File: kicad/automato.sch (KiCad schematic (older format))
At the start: 72 parts, among them J1 USB_C_Receptacle, J10 QWIIC 0, J2 LiPo, J3 Conn_01x07_Male, J4 Screw_Terminal_01x15, J5 USB_C_Receptacle, J6 Conn_Coaxial, J7 UART2 0, J8 Micro_SD_Card_Det, J9 UART2 1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

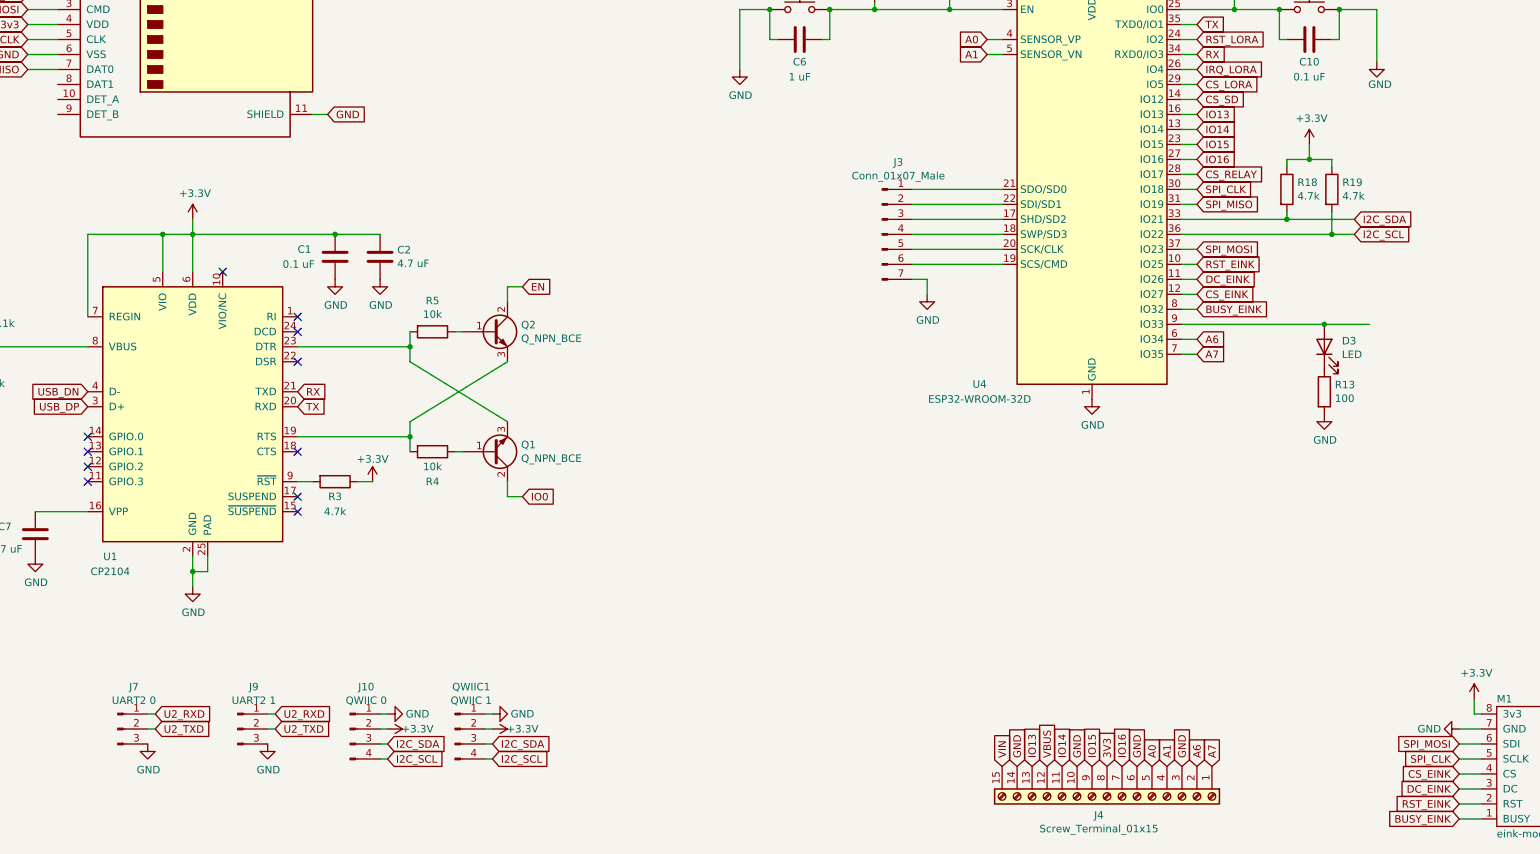
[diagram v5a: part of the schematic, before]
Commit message: adding more jst connectors, moving pin assignments
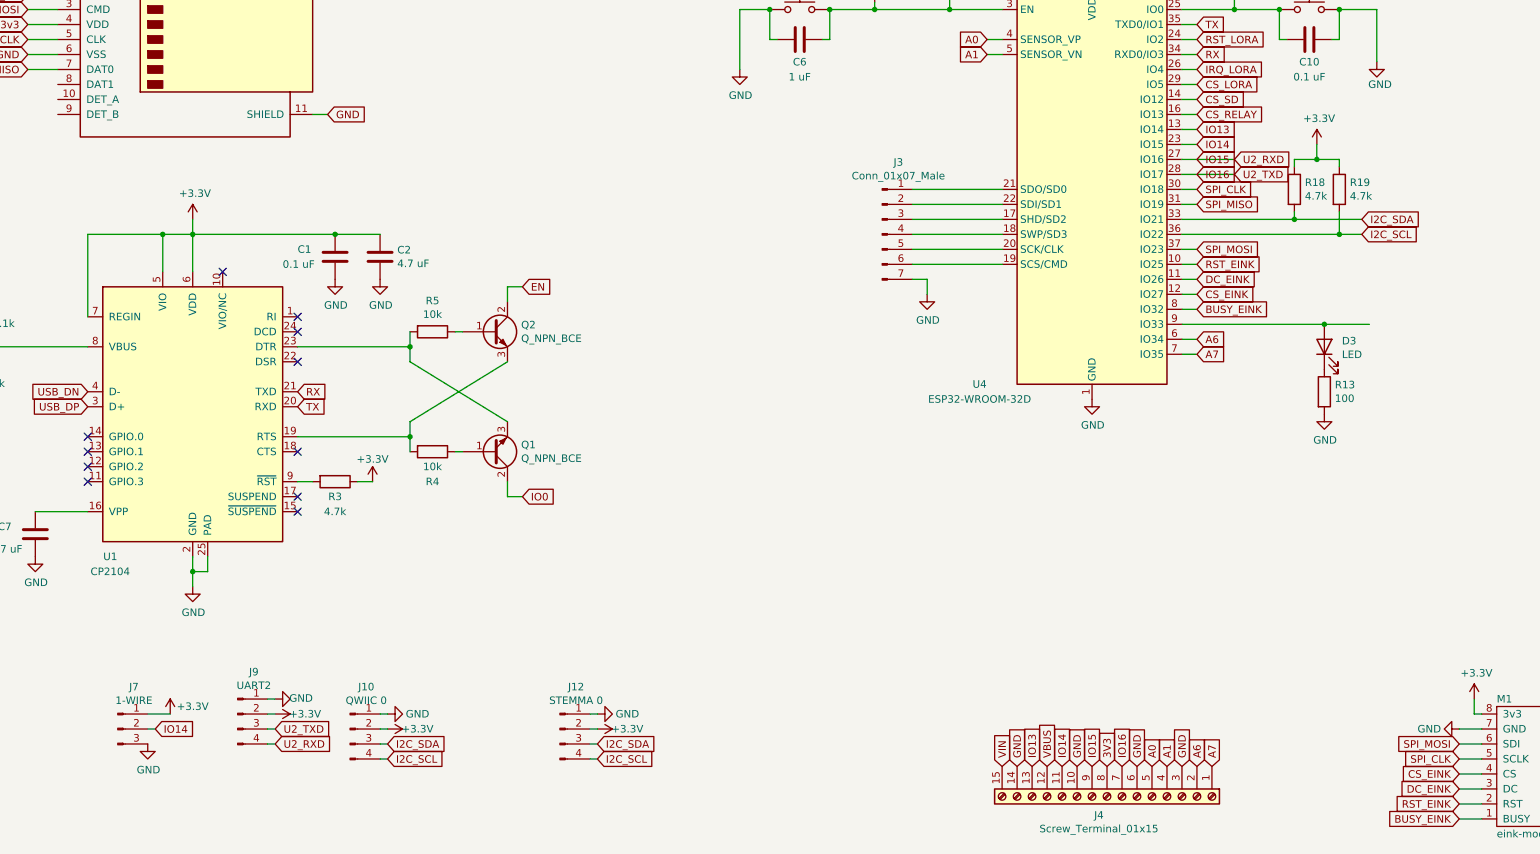
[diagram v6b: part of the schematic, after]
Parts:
- removed J9: UART2 1, Connector_JST:JST_PH_S3B-PH-SM4-TB_1x03-1MP_P2.00mm_Horizontal, symbol Connector:Conn_01x03_Male
- removed QWIIC1: QWIIC 1, Connector_JST:JST_SH_SM04B-SRSS-TB_1x04-1MP_P1.00mm_Horizontal, symbol Connector:Conn_01x04_Male
- added J12: STEMMA 0, Connector_JST:JST_PH_S4B-PH-SM4-TB_1x04-1MP_P2.00mm_Horizontal, symbol Connector:Conn_01x04_Male
- added J9: UART2, Connector_JST:JST_PH_S4B-PH-SM4-TB_1x04-1MP_P2.00mm_Horizontal, symbol Connector:Conn_01x04_Male
- J6: footprint Connector_Coaxial:SMA_Wurth_60312002114503_Vertical -> Connector_Coaxial:SMA_Molex_73251-1153_EdgeMount_Horizontal
- J7: value UART2 0 -> 1-WIRE
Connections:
- net +3V3: now also J7.1 (Pin_1), J12.2 (Pin_2), J9.2 (Pin_2)
- net CS_RELAY: now also U4.16 (IO13); no longer U4.28 (IO17)
- net GND: now also J12.1 (Pin_1), J9.1 (Pin_1)
- net I2C_SCL: now also J12.4 (Pin_4)
- net I2C_SDA: now also J12.3 (Pin_3)
- net IO13: now also U4.13 (IO14); no longer U4.16 (IO13)
- net IO14: now also J7.2 (Pin_2), U4.23 (IO15); no longer U4.13 (IO14)
- net IO15: now also JP1.3 (B), U4.27 (IO16), J9.4 (Pin_4); no longer U4.23 (IO15)
- net IO16: now also JP2.3 (B), U4.28 (IO17), J9.3 (Pin_3); no longer U4.27 (IO16)
- removed net U2_RXD: J7.1 (Pin_1), JP1.3 (B)
- removed net U2_TXD: J7.2 (Pin_2), JP2.3 (B)
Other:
- moved on the sheet: R18, R19
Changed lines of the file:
@@
 Wire Wire Line
 	9550 5350 9650 5350
-Text GLabel 9650 5350 2    50   Input ~ 0
-CS_SD
 Text GLabel 9650 5950 2    50   Input ~ 0
 SPI_CLK
 Text GLabel 9650 6050 2    50   Input ~ 0
 SPI_MISO
-Text GLabel 10700 6150 2    50   Input ~ 0
+Text GLabel 10750 6150 2    50   Input ~ 0
 I2C_SDA
-Text GLabel 10700 6250 2    50   Input ~ 0
+Text GLabel 10750 6250 2    50   Input ~ 0
 I2C_SCL
 Text GLabel 9650 6350 2    50   Input ~ 0
 SPI_MOSI
-Text GLabel 9650 5750 2    50   Input ~ 0
-IO16
-Text GLabel 9650 5450 2    50   Input ~ 0
-IO13
-Text GLabel 9650 5550 2    50   Input ~ 0
-IO14
 Text GLabel 9650 6950 2    50   Input ~ 0
 A6
@@
 	9550 5650 9650 5650
 Wire Wire Line
-	9550 5750 9650 5750
-Wire Wire Line
-	9550 5850 9650 5850
-Wire Wire Line
 	9550 5950 9650 5950
 Wire Wire Line
 	9550 6050 9650 6050
-Wire Wire Line
-	9550 6150 10250 6150
 Wire Wire Line
 	9550 6350 9650 6350
@@
 L Device:R R18
 U 1 1 6005DDCE
-P 10250 5950
-F 0 "R18" H 10320 5996 50  0000 L CNN
-F 1 "4.7k" H 10320 5905 50  0000 L CNN
-F 2 "Resistor_SMD:R_0805_2012Metric" V 10180 5950 50  0001 C CNN
-F 3 "~" H 10250 5950 50  0001 C CNN
-	1    10250 5950
+P 10300 5950
+F 0 "R18" H 10370 5996 50  0000 L CNN
+F 1 "4.7k" H 10370 5905 50  0000 L CNN
+F 2 "Resistor_SMD:R_0805_2012Metric" V 10230 5950 50  0001 C CNN
+F 3 "~" H 10300 5950 50  0001 C CNN
+	1    10300 5950
 	1    0    0    -1
 $EndComp
@@
 L Device:R R19
 U 1 1 6005E3C7
-P 10550 5950
-F 0 "R19" H 10620 5996 50  0000 L CNN
-F 1 "4.7k" H 10620 5905 50  0000 L CNN
-F 2 "Resistor_SMD:R_0805_2012Metric" V 10480 5950 50  0001 C CNN
-F 3 "~" H 10550 5950 50  0001 C CNN
-	1    10550 5950
-	1    0    0    -1
-$EndComp
-Wire Wire Line
-	10250 6100 10250 6150
-Connection ~ 10250 6150
-Wire Wire Line
-	10250 6150 10700 6150
+P 10600 5950
+F 0 "R19" H 10670 5996 50  0000 L CNN
+F 1 "4.7k" H 10670 5905 50  0000 L CNN
+F 2 "Resistor_SMD:R_0805_2012Metric" V 10530 5950 50  0001 C CNN
+F 3 "~" H 10600 5950 50  0001 C CNN
+	1    10600 5950
+	1    0    0    -1
+$EndComp
+Wire Wire Line
+	10300 6100 10300 6150
+Connection ~ 10300 6150
+Wire Wire Line
+	10300 6150 10750 6150
 $Comp
 L power:+3.3V #PWR03
 U 1 1 6009B289
-P 10400 5650
-F 0 "#PWR03" H 10400 5500 50  0001 C CNN
-F 1 "+3.3V" H 10415 5823 50  0000 C CNN
-F 2 "" H 10400 5650 50  0001 C CNN
-F 3 "" H 10400 5650 50  0001 C CNN
-	1    10400 5650
-	1    0    0    -1
-$EndComp
-Wire Wire Line
-	9550 6250 10550 6250
-Wire Wire Line
-	10550 6100 10550 6250
-Connection ~ 10550 6250
-Wire Wire Line
-	10550 6250 10700 6250
-Wire Wire Line
-	10250 5800 10250 5750
-Wire Wire Line
-	10250 5750 10400 5750
-Wire Wire Line
-	10400 5750 10400 5650
-Wire Wire Line
-	10400 5750 10550 5750
-Wire Wire Line
-	10550 5750 10550 5800
-Connection ~ 10400 5750
+P 10450 5650
+F 0 "#PWR03" H 10450 5500 50  0001 C CNN
+F 1 "+3.3V" H 10465 5823 50  0000 C CNN
+F 2 "" H 10450 5650 50  0001 C CNN
+F 3 "" H 10450 5650 50  0001 C CNN
+	1    10450 5650
+	1    0    0    -1
+$EndComp
+Wire Wire Line
+	10600 6100 10600 6250
+Connection ~ 10600 6250
+Wire Wire Line
+	10600 6250 10750 6250
+Wire Wire Line
+	10300 5800 10300 5750
+Wire Wire Line
+	10300 5750 10450 5750
+Wire Wire Line
+	10450 5750 10450 5650
+Wire Wire Line
+	10450 5750 10600 5750
+Wire Wire Line
+	10600 5750 10600 5800
+Connection ~ 10450 5750
 $Comp
 L Connector:TestPoint TP1
@@
 Wire Wire Line
 	4550 1200 4550 1250
-Text GLabel 9650 5650 2    50   Input ~ 0
-IO15
 $Comp
 L automato-sensor:eink-module M1
@@
 F 0 "J6" H 16250 5825 50  0000 L CNN
 F 1 "Conn_Coaxial" H 16250 5734 50  0000 L CNN
-F 2 "Connector_Coaxial:SMA_Wurth_60312002114503_Vertical" H 16150 5850 50  0001 C CNN
+F 2 "Connector_Coaxial:SMA_Molex_73251-1153_EdgeMount_Horizontal" H 16150 5850 50  0001 C CNN
 F 3 " ~" H 16150 5850 50  0001 C CNN
 	1    16150 5850
@@
 	1    0    0    -1
 $EndComp
-Text GLabel 9650 5850 2    50   Input ~ 0
+Text GLabel 9650 5450 2    50   Input ~ 0
 CS_RELAY
 $Comp
@@
 $EndComp
 $Comp
-L Connector:Conn_01x03_Male J7
-U 1 1 632E9370
-P 2450 9550
-F 0 "J7" H 2558 9831 50  0000 C CNN
-F 1 "UART2 0" H 2558 9740 50  0000 C CNN
-F 2 "Connector_JST:JST_PH_S3B-PH-SM4-TB_1x03-1MP_P2.00mm_Horizontal" H 2450 9550 50  0001 C CNN
-F 3 "~" H 2450 9550 50  0001 C CNN
-	1    2450 9550
-	1    0    0    -1
-$EndComp
-$Comp
-L Connector:Conn_01x03_Male J9
-U 1 1 632E9C6B
-P 3250 9550
-F 0 "J9" H 3358 9831 50  0000 C CNN
-F 1 "UART2 1" H 3358 9740 50  0000 C CNN
-F 2 "Connector_JST:JST_PH_S3B-PH-SM4-TB_1x03-1MP_P2.00mm_Horizontal" H 3250 9550 50  0001 C CNN
-F 3 "~" H 3250 9550 50  0001 C CNN
-	1    3250 9550
-	1    0    0    -1
-$EndComp
-$Comp
 L power:GND #PWR0105
 U 1 1 632EA398
@@
 L power:GND #PWR0106
 U 1 1 632EBE7A
-P 3450 9650
-F 0 "#PWR0106" H 3450 9400 50  0001 C CNN
-F 1 "GND" H 3455 9477 50  0000 C CNN
-F 2 "" H 3450 9650 50  0001 C CNN
-F 3 "" H 3450 9650 50  0001 C CNN
-	1    3450 9650
-	1    0    0    -1
-$EndComp
-Text GLabel 2700 9450 2    50   Input ~ 0
-U2_RXD
-Text GLabel 2700 9550 2    50   Input ~ 0
-U2_TXD
+P 3500 9350
+F 0 "#PWR0106" H 3500 9100 50  0001 C CNN
+F 1 "GND" V 3505 9177 50  0000 C CNN
+F 2 "" H 3500 9350 50  0001 C CNN
+F 3 "" H 3500 9350 50  0001 C CNN
+	1    3500 9350
+	0    -1   -1   0
+$EndComp
 Wire Wire Line
 	2700 9550 2650 9550
-Wire Wire Line
-	2700 9450 2650 9450
-Text GLabel 3500 9450 2    50   Input ~ 0
+Text GLabel 3500 9650 2    50   Input ~ 0
 U2_RXD
 Text GLabel 3500 9550 2    50   Input ~ 0
@@
 	0    1    1    0
 $EndComp
-$Comp
-L Connector:Conn_01x04_Male QWIIC1
-U 1 1 633A41C7
-P 4700 9550
-F 0 "QWIIC1" H 4808 9831 50  0000 C CNN
-F 1 "QWIIC 1" H 4808 9740 50  0000 C CNN
-F 2 "Connector_JST:JST_SH_SM04B-SRSS-TB_1x04-1MP_P1.00mm_Horizontal" H 4700 9550 50  0001 C CNN
-F 3 "~" H 4700 9550 50  0001 C CNN
-	1    4700 9550
-	1    0    0    -1
-$EndComp
-Text GLabel 4950 9750 2    50   Input ~ 0
-I2C_SCL
-Text GLabel 4950 9650 2    50   Input ~ 0
-I2C_SDA
-Wire Wire Line
-	4950 9750 4900 9750
-Wire Wire Line
-	4900 9650 4950 9650
-Wire Wire Line
-	4900 9450 4950 9450
-Wire Wire Line
-	4900 9550 4950 9550
-$Comp
-L power:GND #PWR0109
-U 1 1 633A41D3
-P 4950 9450
-F 0 "#PWR0109" H 4950 9200 50  0001 C CNN
-F 1 "GND" V 4950 9250 50  0000 C CNN
-F 2 "" H 4950 9450 50  0001 C CNN
-F 3 "" H 4950 9450 50  0001 C CNN
-	1    4950 9450
-	0    -1   -1   0
-$EndComp
-$Comp
-L power:+3.3V #PWR0110
-U 1 1 633A41D9
-P 4950 9550
-F 0 "#PWR0110" H 4950 9400 50  0001 C CNN
-F 1 "+3.3V" V 4950 9750 50  0000 C CNN
-F 2 "" H 4950 9550 50  0001 C CNN
-F 3 "" H 4950 9550 50  0001 C CNN
-	1    4950 9550
-	0    1    1    0
-$EndComp
 Wire Wire Line
 	15250 5850 15950 5850
@@
 Text GLabel 9550 9800 1    50   Input ~ 0
 GND
+$Comp
+L Connector:Conn_01x04_Male J12
+U 1 1 62ECA939
+P 5400 9550
+F 0 "J12" H 5508 9831 50  0000 C CNN
+F 1 "STEMMA 0" H 5508 9740 50  0000 C CNN
+F 2 "Connector_JST:JST_PH_S4B-PH-SM4-TB_1x04-1MP_P2.00mm_Horizontal" H 5400 9550 50  0001 C CNN
+F 3 "~" H 5400 9550 50  0001 C CNN
+	1    5400 9550
+	1    0    0    -1
+$EndComp
+Text GLabel 5650 9750 2    50   Input ~ 0
+I2C_SCL
+Text GLabel 5650 9650 2    50   Input ~ 0
+I2C_SDA
+Wire Wire Line
+	5650 9750 5600 9750
+Wire Wire Line
+	5600 9650 5650 9650
+Wire Wire Line
+	5600 9450 5650 9450
+Wire Wire Line
+	5600 9550 5650 9550
+$Comp
+L power:GND #PWR0112
+U 1 1 62ECA945
+P 5650 9450
+F 0 "#PWR0112" H 5650 9200 50  0001 C CNN
+F 1 "GND" V 5650 9250 50  0000 C CNN
+F 2 "" H 5650 9450 50  0001 C CNN
+F 3 "" H 5650 9450 50  0001 C CNN
+	1    5650 9450
+	0    -1   -1   0
+$EndComp
+$Comp
+L power:+3.3V #PWR0113
+U 1 1 62ECA94B
+P 5650 9550
+F 0 "#PWR0113" H 5650 9400 50  0001 C CNN
+F 1 "+3.3V" V 5650 9750 50  0000 C CNN
+F 2 "" H 5650 9550 50  0001 C CNN
+F 3 "" H 5650 9550 50  0001 C CNN
+	1    5650 9550
+	0    1    1    0
+$EndComp
+Text GLabel 9900 5850 2    50   Input ~ 0
+U2_TXD
+Text GLabel 9650 5750 2    50   Input ~ 0
+IO15
+Text GLabel 9650 5650 2    50   Input ~ 0
+IO14
+Text GLabel 9650 5550 2    50   Input ~ 0
+IO13
+Text GLabel 9650 5850 2    50   Input ~ 0
+IO16
+Text GLabel 9650 5350 2    50   Input ~ 0
+CS_SD
+Text GLabel 9900 5750 2    50   Input ~ 0
+U2_RXD
+Wire Wire Line
+	9550 5750 9900 5750
+Wire Wire Line
+	9550 5850 9900 5850
+Wire Wire Line
+	9550 6150 10300 6150
+Wire Wire Line
+	9550 6250 10600 6250
+Text GLabel 2700 9550 2    50   Input ~ 0
+IO14
+$Comp
+L power:+3.3V #PWR0109
+U 1 1 6309946C
+P 2800 9450
+F 0 "#PWR0109" H 2800 9300 50  0001 C CNN
+F 1 "+3.3V" H 2950 9500 50  0000 C CNN
+F 2 "" H 2800 9450 50  0001 C CNN
+F 3 "" H 2800 9450 50  0001 C CNN
+	1    2800 9450
+	1    0    0    -1
+$EndComp
+$Comp
+L Connector:Conn_01x03_Male J7
+U 1 1 632E9370
+P 2450 9550
+F 0 "J7" H 2558 9831 50  0000 C CNN
+F 1 "1-WIRE" H 2558 9740 50  0000 C CNN
+F 2 "Connector_JST:JST_PH_S3B-PH-SM4-TB_1x03-1MP_P2.00mm_Horizontal" H 2450 9550 50  0001 C CNN
+F 3 "~" H 2450 9550 50  0001 C CNN
+	1    2450 9550
+	1    0    0    -1
+$EndComp
+$Comp
+L Connector:Conn_01x04_Male J9
+U 1 1 630F935A
+P 3250 9450
+F 0 "J9" H 3358 9731 50  0000 C CNN
+F 1 "UART2" H 3358 9640 50  0000 C CNN
+F 2 "Connector_JST:JST_PH_S4B-PH-SM4-TB_1x04-1MP_P2.00mm_Horizontal" H 3250 9450 50  0001 C CNN
+F 3 "~" H 3250 9450 50  0001 C CNN
+	1    3250 9450
+	1    0    0    -1
+$EndComp
+$Comp
+L power:+3.3V #PWR0110
+U 1 1 630FA4D3
+P 3500 9450
+F 0 "#PWR0110" H 3500 9300 50  0001 C CNN
+F 1 "+3.3V" V 3500 9650 50  0000 C CNN
+F 2 "" H 3500 9450 50  0001 C CNN
+F 3 "" H 3500 9450 50  0001 C CNN
+	1    3500 9450
+	0    1    1    0
+$EndComp
+Wire Wire Line
+	3450 9350 3500 9350
+Wire Wire Line
+	2650 9450 2800 9450
+Wire Wire Line
+	3500 9650 3450 9650
 $EndSCHEMATC

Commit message: change tactile switch footprint
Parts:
- SW1, SW2: footprint Button_Switch_SMD:SW_Push_1P1T_NO_6x6mm_H9.5mm -> Button_Switch_SMD:SW_SPST_EVQPE1
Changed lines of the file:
@@
 F 0 "SW2" H 10400 5035 50  0000 C CNN
 F 1 "SW_Push" H 10400 4950 50  0000 C CNN
-F 2 "Button_Switch_SMD:SW_Push_1P1T_NO_6x6mm_H9.5mm" H 10400 4950 50  0001 C CNN
+F 2 "Button_Switch_SMD:SW_SPST_EVQPE1" H 10400 4950 50  0001 C CNN
 F 3 "~" H 10400 4950 50  0001 C CNN
 	1    10400 4750
@@
 F 0 "SW1" H 7000 5035 50  0000 C CNN
 F 1 "SW_Push" H 7000 4944 50  0000 C CNN
-F 2 "Button_Switch_SMD:SW_Push_1P1T_NO_6x6mm_H9.5mm" H 7000 4950 50  0001 C CNN
+F 2 "Button_Switch_SMD:SW_SPST_EVQPE1" H 7000 4950 50  0001 C CNN
 F 3 "~" H 7000 4950 50  0001 C CNN
 	1    7000 4750

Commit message: finish JST route
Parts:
- added J11: UART2, Connector_JST:JST_PH_S4B-PH-SM4-TB_1x04-1MP_P2.00mm_Horizontal, symbol Connector:Conn_01x04_Male
- J4: value Screw_Terminal_01x15 -> Screw_Terminal_01x14; footprint TerminalBlock_Phoenix:TerminalBlock_Phoenix_PT-1,5-15-3.5-H_1x15_P3.50mm_Horizontal -> TerminalBlock_Phoenix:TerminalBlock_Phoenix_PT-1,5-14-3.5-H_1x14_P3.50mm_Horizontal; symbol Connector:Screw_Terminal_01x15 -> Connector:Screw_Terminal_01x14
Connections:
- net labels removed: 3V3, 3v3
- wire segments 266 -> 269
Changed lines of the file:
@@
 Comment4 ""
 $EndDescr
+Text GLabel 9550 9800 1    50   Input ~ 0
+A6
 Text GLabel 9650 9800 1    50   Input ~ 0
-A6
-Text GLabel 9750 9800 1    50   Input ~ 0
 A7
 Text GLabel 11400 9650 0    50   Input ~ 0
@@
 F 3 "~" H 15100 2750 50  0001 C CNN
 	1    15100 2750
-	-1   0    0    1
+	-1   0    0    -1
 $EndComp
 Wire Wire Line
@@
 Text GLabel 9250 9800 1    50   Input ~ 0
 GND
-Text GLabel 9050 9800 1    50   Input ~ 0
-3V3
 $Comp
 L Device:D_Schottky_Small D1
@@
 Wire Wire Line
 	12100 2000 12300 2000
-Text GLabel 15500 2750 2    50   Input ~ 0
-3V3
-Wire Wire Line
-	15400 2750 15500 2750
 Wire Wire Line
 	12600 7750 12700 7750
@@
 	3800 3550 3800 3600
 $Comp
-L Connector:Screw_Terminal_01x15 J4
+L Connector:Screw_Terminal_01x14 J4
 U 1 1 60071AD4
-P 9050 10000
-F 0 "J4" V 9175 9946 50  0000 C CNN
-F 1 "Screw_Terminal_01x15" V 9266 9946 50  0000 C CNN
-F 2 "TerminalBlock_Phoenix:TerminalBlock_Phoenix_PT-1,5-15-3.5-H_1x15_P3.50mm_Horizontal" H 9050 10000 50  0001 C CNN
-F 3 "~" H 9050 10000 50  0001 C CNN
-	1    9050 10000
-	0    1    1    0
+P 8950 10000
+F 0 "J4" V 9075 9946 50  0000 C CNN
+F 1 "Screw_Terminal_01x14" V 9166 9946 50  0000 C CNN
+F 2 "TerminalBlock_Phoenix:TerminalBlock_Phoenix_PT-1,5-14-3.5-H_1x14_P3.50mm_Horizontal" H 8950 10000 50  0001 C CNN
+F 3 "~" H 8950 10000 50  0001 C CNN
+	1    8950 10000
+	0    -1   1    0
 $EndComp
 Wire Wire Line
@@
 Text GLabel 1850 4750 0    50   Input ~ 0
 SPI_MOSI
-Text GLabel 1850 4850 0    50   Input ~ 0
-3v3
 Text GLabel 1850 4950 0    50   Input ~ 0
 SPI_CLK
@@
 	1    0    0    -1
 $EndComp
-Text GLabel 9550 9800 1    50   Input ~ 0
-GND
 $Comp
 L Connector:Conn_01x04_Male J12
@@
 Wire Wire Line
 	3500 9650 3450 9650
+$Comp
+L power:GND #PWR0114
+U 1 1 63277429
+P 1950 9350
+F 0 "#PWR0114" H 1950 9100 50  0001 C CNN
+F 1 "GND" V 1955 9177 50  0000 C CNN
+F 2 "" H 1950 9350 50  0001 C CNN
+F 3 "" H 1950 9350 50  0001 C CNN
+	1    1950 9350
+	0    -1   -1   0
+$EndComp
+Text GLabel 1950 9650 2    50   Input ~ 0
+RX
+Text GLabel 1950 9550 2    50   Input ~ 0
+TX
+Wire Wire Line
+	1950 9550 1900 9550
+Wire Wire Line
+	1950 9450 1900 9450
+$Comp
+L Connector:Conn_01x04_Male J11
+U 1 1 63277433
+P 1700 9450
+F 0 "J11" H 1808 9731 50  0000 C CNN
+F 1 "UART2" H 1808 9640 50  0000 C CNN
+F 2 "Connector_JST:JST_PH_S4B-PH-SM4-TB_1x04-1MP_P2.00mm_Horizontal" H 1700 9450 50  0001 C CNN
+F 3 "~" H 1700 9450 50  0001 C CNN
+	1    1700 9450
+	1    0    0    -1
+$EndComp
+$Comp
+L power:+3.3V #PWR0115
+U 1 1 63277439
+P 1950 9450
+F 0 "#PWR0115" H 1950 9300 50  0001 C CNN
+F 1 "+3.3V" V 1950 9650 50  0000 C CNN
+F 2 "" H 1950 9450 50  0001 C CNN
+F 3 "" H 1950 9450 50  0001 C CNN
+	1    1950 9450
+	0    1    1    0
+$EndComp
+Wire Wire Line
+	1900 9350 1950 9350
+Wire Wire Line
+	1950 9650 1900 9650
+$Comp
+L power:+3.3V #PWR0116
+U 1 1 632EA34B
+P 9050 9800
+F 0 "#PWR0116" H 9050 9650 50  0001 C CNN
+F 1 "+3.3V" V 9050 10000 50  0000 C CNN
+F 2 "" H 9050 9800 50  0001 C CNN
+F 3 "" H 9050 9800 50  0001 C CNN
+	1    9050 9800
+	1    0    0    -1
+$EndComp
+$Comp
+L power:+3.3V #PWR0117
+U 1 1 632EAC68
+P 1850 4850
+F 0 "#PWR0117" H 1850 4700 50  0001 C CNN
+F 1 "+3.3V" V 1850 5100 50  0000 C CNN
+F 2 "" H 1850 4850 50  0001 C CNN
+F 3 "" H 1850 4850 50  0001 C CNN
+	1    1850 4850
+	0    -1   -1   0
+$EndComp
 $EndSCHEMATC
